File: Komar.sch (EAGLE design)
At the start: 112 parts, among them CON1 USB-VERTICAL, CON10 PINHEAD_1X01-2, CON11 PINHEAD_1X01-2, CON12 PINHEAD_1X01-2, CON13 PINHEAD_1X01-2, CON14 PINHEAD_1X01-2, CON15 PINHEAD_1X01-2, CON2 PINHEAD_1X01-2, CON3 CON-4P-TABS-STRAIGHT, CON4 CON-4P-TABS-STRAIGHT, CON5 CON-4P-TABS-STRAIGHT, CON6 CON-4P-TABS-STRAIGHT, CON7 CON-4P-TABS-STRAIGHT, CON8 PINHEAD_1X04-2, CON9 PINHEAD_1X01-2, IC1 TPD3S014DBVR-SOT23-6, IC2 TPD3S014DBVR-SOT23-6, IC3 ATA6561-GBQW-N-HVSON8, IC4 ATA6561-GBQW-N-HVSON8, IC5 MCP9700AT-E/TTVAO-SOT23, IC6 11LC040T-E/TT, Q1 FDMS86368-F085, Q10 FDMS86368-F085, Q11 FDMS86368-F085, Q12 FDMS86368-F085, Q2 FDMS86368-F085, Q3 FDMS86368-F085, Q4 FDMS86368-F085, Q5 FDMS86368-F085, Q6 FDMS86368-F085, Q7 FDMS86368-F085, Q8 FDMS86368-F085, Q9 FDMS86368-F085

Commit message: minor attribute update
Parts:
- R10, R11, R12, R13, R26, R6, R9: DIGIKEY# P1.0KGCT-ND -> P1.00KLCT-ND; MANF# ERJ-3GEYJ102V -> ERJ-2RKF1001X
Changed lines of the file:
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@@
 </attributes>
 <variantdefs>
-<variantdef name="BASIC"/>
+<variantdef name="BASIC" current="yes"/>
 </variantdefs>
 <classes>
@@
 <part name="R11" library="rc" library_urn="urn:adsk.eagle:library:2539423" deviceset="R" device="-0402" package3d_urn="urn:adsk.eagle:package:2539456/2" technology="-5%" value="1K">
 <attribute name="AEC-Q" value="AEC-Q200"/>
-<attribute name="DIGIKEY#" value="P1.0KGCT-ND"/>
-<attribute name="MANF" value="Panasonic Electronic Components"/>
-<attribute name="MANF#" value="ERJ-3GEYJ102V"/>
+<attribute name="DIGIKEY#" value="P1.00KLCT-ND"/>
+<attribute name="MANF" value="Panasonic Electronic Components"/>
+<attribute name="MANF#" value="ERJ-2RKF1001X"/>
 <attribute name="OPERATING_TEMP" value="-55°C ~ 155°C"/>
 </part>
 <part name="R12" library="rc" library_urn="urn:adsk.eagle:library:2539423" deviceset="R" device="-0402" package3d_urn="urn:adsk.eagle:package:2539456/2" technology="-5%" value="1K">
 <attribute name="AEC-Q" value="AEC-Q200"/>
-<attribute name="DIGIKEY#" value="P1.0KGCT-ND"/>
-<attribute name="MANF" value="Panasonic Electronic Components"/>
-<attribute name="MANF#" value="ERJ-3GEYJ102V"/>
+<attribute name="DIGIKEY#" value="P1.00KLCT-ND"/>
+<attribute name="MANF" value="Panasonic Electronic Components"/>
+<attribute name="MANF#" value="ERJ-2RKF1001X"/>
 <attribute name="OPERATING_TEMP" value="-55°C ~ 155°C"/>
 </part>
 <part name="R13" library="rc" library_urn="urn:adsk.eagle:library:2539423" deviceset="R" device="-0402" package3d_urn="urn:adsk.eagle:package:2539456/2" technology="-5%" value="1K">
 <attribute name="AEC-Q" value="AEC-Q200"/>
-<attribute name="DIGIKEY#" value="P1.0KGCT-ND"/>
-<attribute name="MANF" value="Panasonic Electronic Components"/>
-<attribute name="MANF#" value="ERJ-3GEYJ102V"/>
+<attribute name="DIGIKEY#" value="P1.00KLCT-ND"/>
+<attribute name="MANF" value="Panasonic Electronic Components"/>
+<attribute name="MANF#" value="ERJ-2RKF1001X"/>
 <attribute name="OPERATING_TEMP" value="-55°C ~ 155°C"/>
 </part>
@@
 <part name="R9" library="rc" library_urn="urn:adsk.eagle:library:2539423" deviceset="R" device="-0402" package3d_urn="urn:adsk.eagle:package:2539456/2" technology="-5%" value="1K">
 <attribute name="AEC-Q" value="AEC-Q200"/>
-<attribute name="DIGIKEY#" value="P1.0KGCT-ND"/>
-<attribute name="MANF" value="Panasonic Electronic Components"/>
-<attribute name="MANF#" value="ERJ-3GEYJ102V"/>
+<attribute name="DIGIKEY#" value="P1.00KLCT-ND"/>
+<attribute name="MANF" value="Panasonic Electronic Components"/>
+<attribute name="MANF#" value="ERJ-2RKF1001X"/>
 <attribute name="OPERATING_TEMP" value="-55°C ~ 155°C"/>
 </part>
 <part name="R10" library="rc" library_urn="urn:adsk.eagle:library:2539423" deviceset="R" device="-0402" package3d_urn="urn:adsk.eagle:package:2539456/2" technology="-5%" value="1K">
 <attribute name="AEC-Q" value="AEC-Q200"/>
-<attribute name="DIGIKEY#" value="P1.0KGCT-ND"/>
-<attribute name="MANF" value="Panasonic Electronic Components"/>
-<attribute name="MANF#" value="ERJ-3GEYJ102V"/>
+<attribute name="DIGIKEY#" value="P1.00KLCT-ND"/>
+<attribute name="MANF" value="Panasonic Electronic Components"/>
+<attribute name="MANF#" value="ERJ-2RKF1001X"/>
 <attribute name="OPERATING_TEMP" value="-55°C ~ 155°C"/>
 </part>
@@
 <part name="R6" library="rc" library_urn="urn:adsk.eagle:library:2539423" deviceset="R" device="-0402" package3d_urn="urn:adsk.eagle:package:2539456/2" technology="-5%" value="1K">
 <attribute name="AEC-Q" value="AEC-Q200"/>
-<attribute name="DIGIKEY#" value="P1.0KGCT-ND"/>
-<attribute name="MANF" value="Panasonic Electronic Components"/>
-<attribute name="MANF#" value="ERJ-3GEYJ102V"/>
+<attribute name="DIGIKEY#" value="P1.00KLCT-ND"/>
+<attribute name="MANF" value="Panasonic Electronic Components"/>
+<attribute name="MANF#" value="ERJ-2RKF1001X"/>
 <attribute name="OPERATING_TEMP" value="-55°C ~ 155°C"/>
 </part>
@@
 <part name="R26" library="rc" library_urn="urn:adsk.eagle:library:2539423" deviceset="R" device="-0402" package3d_urn="urn:adsk.eagle:package:2539456/2" technology="-5%" value="1K">
 <attribute name="AEC-Q" value="AEC-Q200"/>
-<attribute name="DIGIKEY#" value="P1.0KGCT-ND"/>
-<attribute name="MANF" value="Panasonic Electronic Components"/>
-<attribute name="MANF#" value="ERJ-3GEYJ102V"/>
-<attribute name="OPERATING_TEMP" value="-55°C ~ 155°C"/>
-</part>
+<attribute name="DIGIKEY#" value="P1.00KLCT-ND"/>
+<attribute name="MANF" value="Panasonic Electronic Components"/>
+<attribute name="MANF#" value="ERJ-2RKF1001X"/>
+<attribute name="OPERATING_TEMP" value="-55°C ~ 155°C"/>
+</part>

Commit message: LED1, LED2 attribute update
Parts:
- LED1, LED2: DIGIKEY# 511-1652-1-ND -> 1830-IN-S42BT5GCT-ND; MANF Rohm Semiconductor -> Inolux; MANF# SML-P11MTT86 -> IN-S42BT5G
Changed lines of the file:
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@@
 </attributes>
 <variantdefs>
-<variantdef name="BASIC" current="yes"/>
+<variantdef name="BASIC"/>
 </variantdefs>
 <classes>
@@
 <attribute name="AEC-Q" value="---"/>
 <attribute name="COLOR" value="GREEN"/>
-<attribute name="DIGIKEY#" value="511-1652-1-ND"/>
-<attribute name="MANF" value="Rohm Semiconductor"/>
-<attribute name="MANF#" value="SML-P11MTT86"/>
+<attribute name="DIGIKEY#" value="1830-IN-S42BT5GCT-ND"/>
+<attribute name="MANF" value="Inolux"/>
+<attribute name="MANF#" value="IN-S42BT5G"/>
 </part>
 <part name="+P5" library="supply_symbols" library_urn="urn:adsk.eagle:library:5017758" deviceset="5V" device=""/>
@@
 <attribute name="AEC-Q" value="---"/>
 <attribute name="COLOR" value="GREEN"/>
-<attribute name="DIGIKEY#" value="511-1652-1-ND"/>
-<attribute name="MANF" value="Rohm Semiconductor"/>
-<attribute name="MANF#" value="SML-P11MTT86"/>
+<attribute name="DIGIKEY#" value="1830-IN-S42BT5GCT-ND"/>
+<attribute name="MANF" value="Inolux"/>
+<attribute name="MANF#" value="IN-S42BT5G"/>
 </part>
 <part name="+P4" library="supply_symbols" library_urn="urn:adsk.eagle:library:5017758" deviceset="5V" device=""/>
@@
 <part name="+P7" library="supply_symbols" library_urn="urn:adsk.eagle:library:5017758" deviceset="VDC" device=""/>
 <part name="+P8" library="supply_symbols" library_urn="urn:adsk.eagle:library:5017758" deviceset="VDC" device=""/>
-<part name="CON1" library="Connectors" library_urn="urn:adsk.eagle:library:3750510" deviceset="USB" device="-VERTICAL" package3d_urn="urn:adsk.eagle:package:4410721/3">
+<part name="CON1" library="Connectors" library_urn="urn:adsk.eagle:library:3750510" deviceset="USB" device="-VERTICAL" package3d_urn="urn:adsk.eagle:package:4410721/4">
 <attribute name="AEC-Q" value="---"/>
 <attribute name="OPERATING_TEMP" value="-35°C ~ 85°C"/>

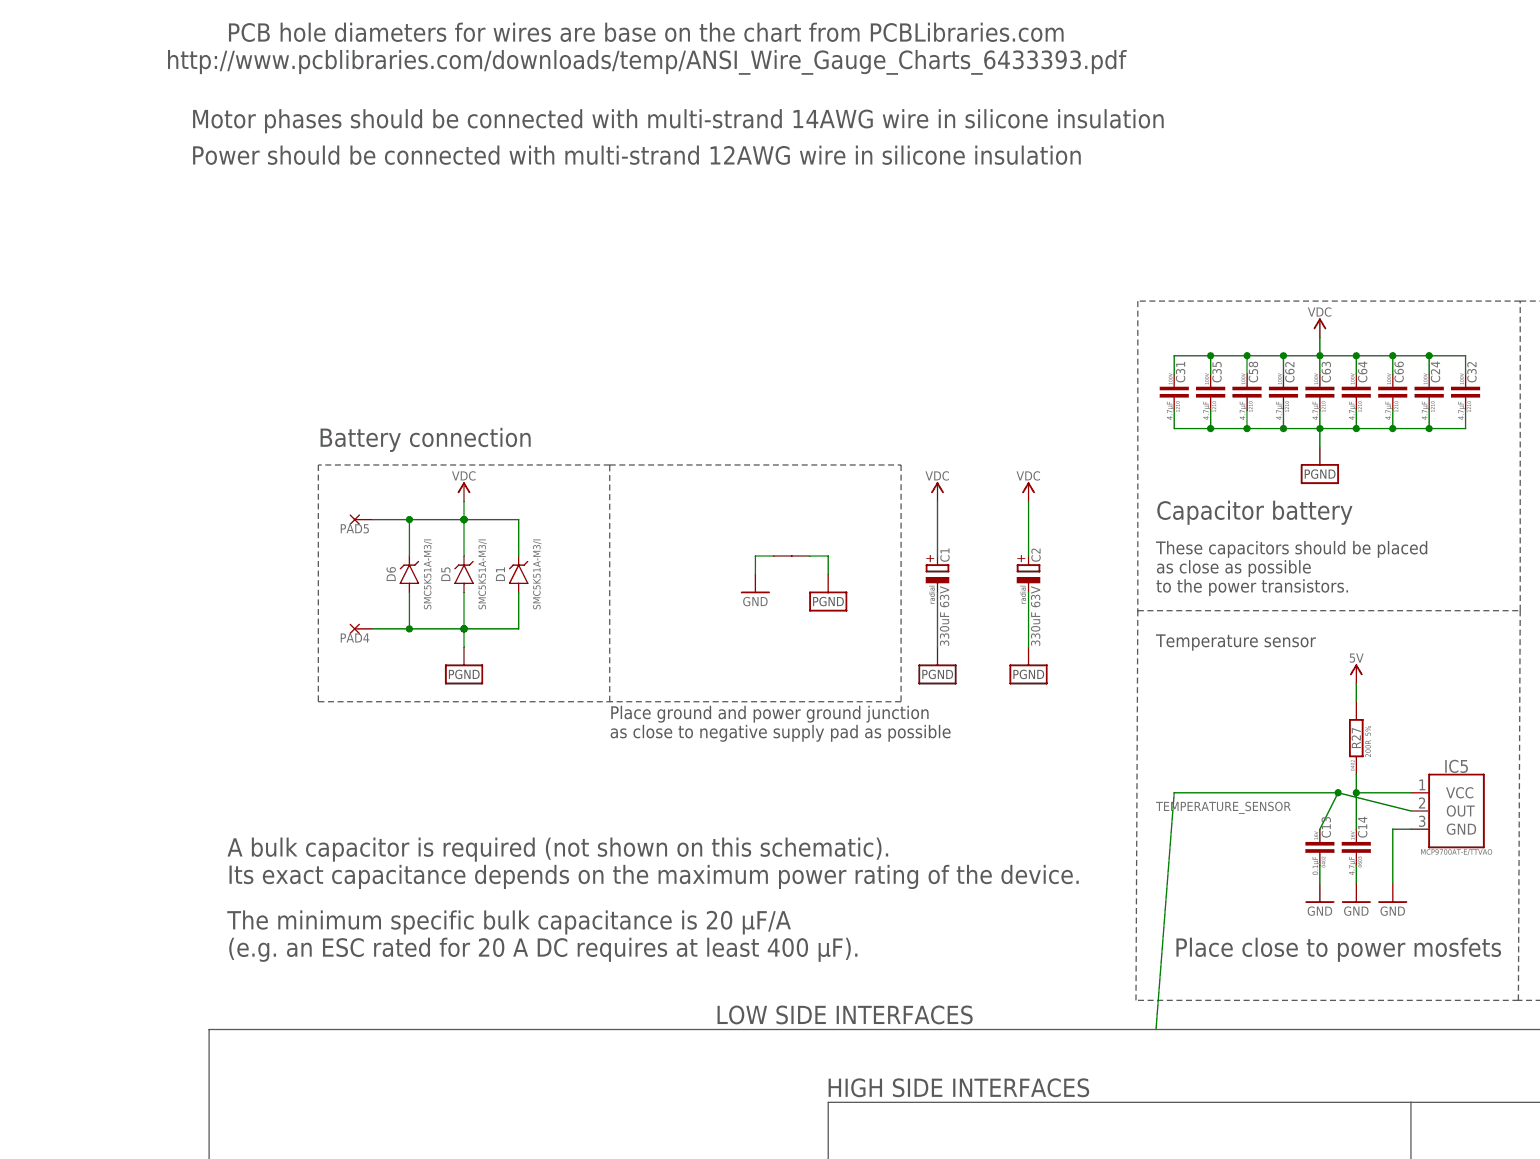
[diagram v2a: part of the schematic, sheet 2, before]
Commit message: minor schematic graphics corrections
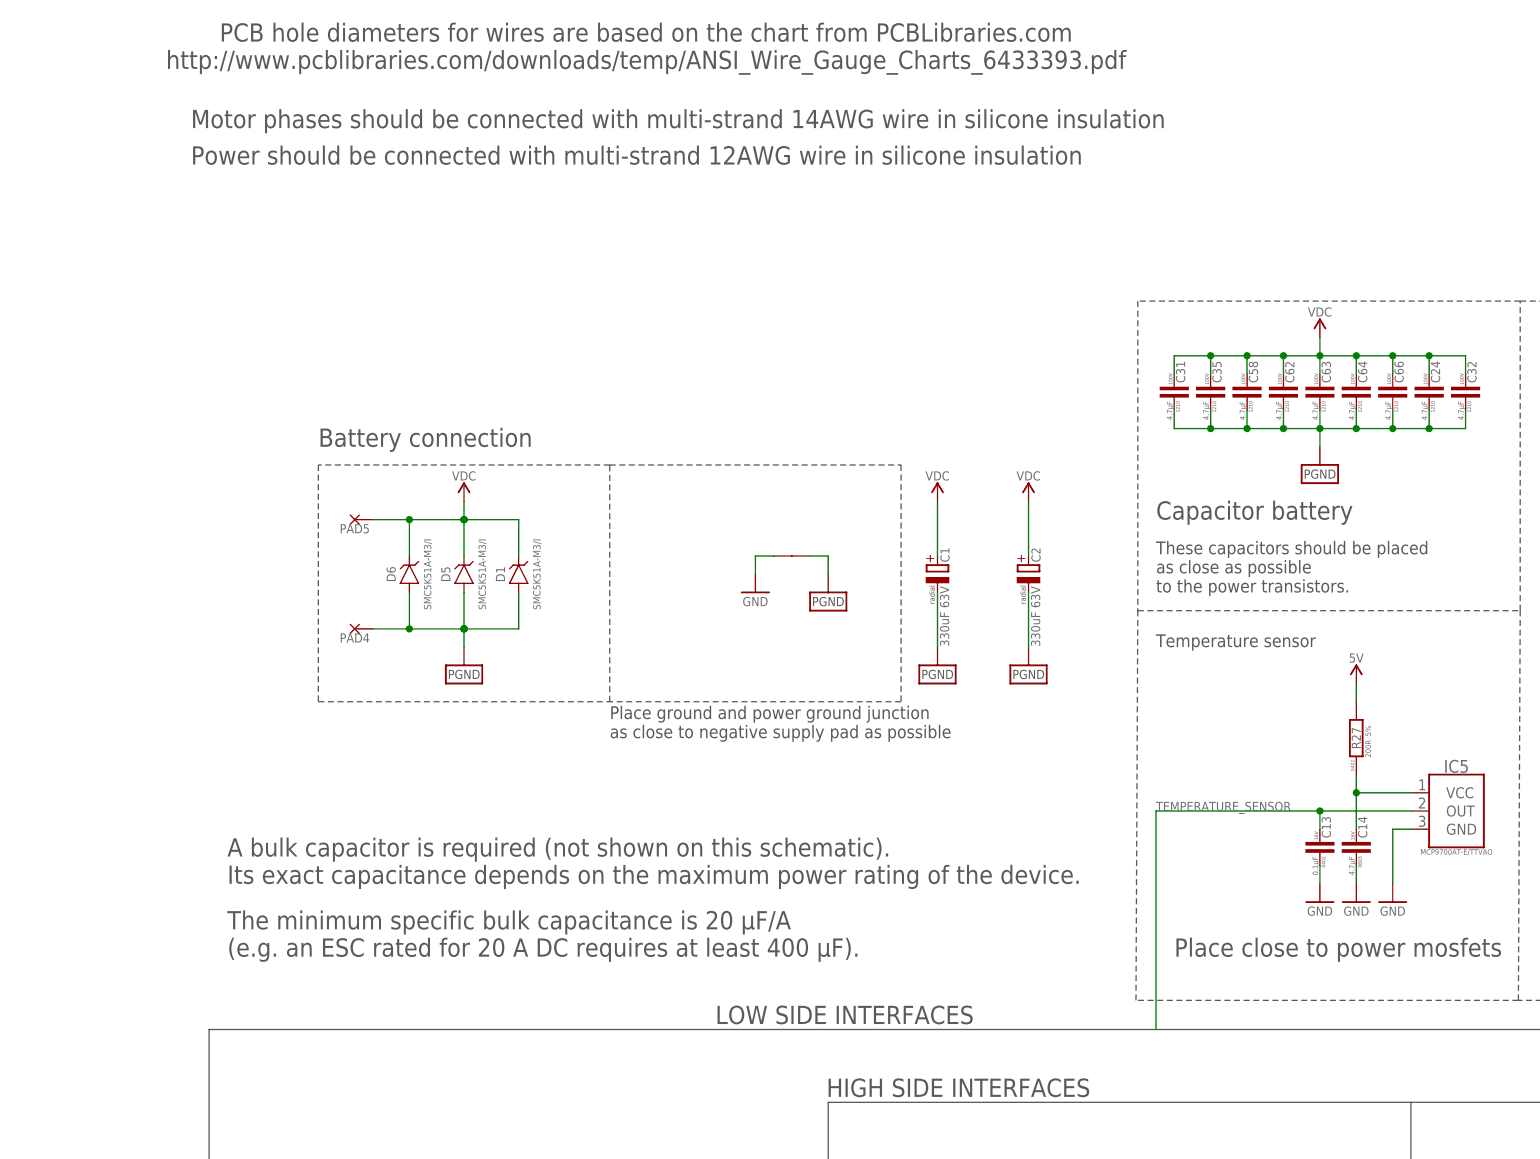
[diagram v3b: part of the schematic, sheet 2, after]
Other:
- note added: "PCB hole diameters for wires are based on the chart from PCBLibraries.com http://www.pcblibraries.com/downloads/temp/ANSI_Wire_Gauge_Charts_6433393.pdf"
- note removed: "PCB hole diameters for wires are base on the chart from PCBLibraries.com http://www.pcblibraries.com/downloads/temp/ANSI_Wire_Gauge_Charts_6433393.pdf"
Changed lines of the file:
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@@
 <text x="5.08" y="276.86" size="2.54" layer="97" font="vector" ratio="15" align="center-left">Motor phases should be connected with multi-strand 14AWG wire in silicone insulation</text>
 <text x="5.08" y="271.78" size="2.54" layer="97" font="vector" ratio="15" align="center-left">Power should be connected with multi-strand 12AWG wire in silicone insulation</text>
-<text x="68.58" y="287.02" size="2.54" layer="97" font="vector" ratio="15" align="center">PCB hole diameters for wires are base on the chart from PCBLibraries.com
+<text x="68.58" y="287.02" size="2.54" layer="97" font="vector" ratio="15" align="center">PCB hole diameters for wires are based on the chart from PCBLibraries.com
 http://www.pcblibraries.com/downloads/temp/ANSI_Wire_Gauge_Charts_6433393.pdf</text>
 </plain>
@@
 <segment>
 <pinref part="IC5" gate="G$1" pin="OUT"/>
-<wire x1="175.26" y1="180.34" x2="165.1" y2="182.88" width="0.1524" layer="91"/>
-<wire x1="162.56" y1="177.8" x2="165.1" y2="182.88" width="0.1524" layer="91"/>
-<junction x="165.1" y="182.88"/>
+<wire x1="175.26" y1="180.34" x2="162.56" y2="180.34" width="0.1524" layer="91"/>
+<wire x1="162.56" y1="177.8" x2="162.56" y2="180.34" width="0.1524" layer="91"/>
+<junction x="162.56" y="180.34"/>
 <pinref part="C13" gate="G$1" pin="2"/>
-<wire x1="142.24" y1="182.88" x2="165.1" y2="182.88" width="0.1524" layer="91"/>
-<wire x1="139.7" y1="149.86" x2="142.24" y2="182.88" width="0.1524" layer="91"/>
+<wire x1="139.7" y1="180.34" x2="162.56" y2="180.34" width="0.1524" layer="91"/>
+<wire x1="139.7" y1="149.86" x2="139.7" y2="180.34" width="0.1524" layer="91"/>
 <label x="139.7" y="180.34" size="1.27" layer="95" font="vector"/>
 </segment>

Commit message: manufacturing instruction update
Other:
- note removed: "Motor phases should be connected with multi-strand 14AWG wire in silicone insulation"
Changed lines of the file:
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@@
 <wire x1="233.68" y1="30.48" x2="233.68" y2="73.66" width="0.1524" layer="97" style="shortdash"/>
 <wire x1="233.68" y1="73.66" x2="180.34" y2="73.66" width="0.1524" layer="97" style="shortdash"/>
-<text x="5.08" y="276.86" size="2.54" layer="97" font="vector" ratio="15" align="center-left">Motor phases should be connected with multi-strand 14AWG wire in silicone insulation</text>
-<text x="5.08" y="271.78" size="2.54" layer="97" font="vector" ratio="15" align="center-left">Power should be connected with multi-strand 12AWG wire in silicone insulation</text>
-<text x="68.58" y="287.02" size="2.54" layer="97" font="vector" ratio="15" align="center">PCB hole diameters for wires are based on the chart from PCBLibraries.com
+<text x="5.08" y="269.24" size="2.54" layer="97" font="vector" ratio="15" align="center-left">Power should be connected with multi-strand 12AWG wire in silicone insulation</text>
+<text x="68.58" y="276.86" size="2.54" layer="97" font="vector" ratio="15" align="center">PCB hole diameters for wires are based on the chart from PCBLibraries.com
 http://www.pcblibraries.com/downloads/temp/ANSI_Wire_Gauge_Charts_6433393.pdf</text>
 </plain>
